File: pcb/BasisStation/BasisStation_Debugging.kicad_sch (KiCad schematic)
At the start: 2 parts, among them J1 USB_B_Micro, U1 D3V3XA4B10LP

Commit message: v0.00.001 chore(SHBS-4): Symbole aus Bibliothek aktualisiert
KiCad-Lauf "Symbole aus Bibliothek aktualisieren" (Bediener): die zuvor per
Text-Edit erzeugte power:+3V3-Cache-Definition wurde durch das
Bibliotheksoriginal ersetzt (abweichende Referenz-Position, Pfeil aus zwei
Polylines), lib_symbols alphabetisch sortiert.

Laut report.txt aktualisieren #PWR100-#PWR102 (power:+3V3), PS1
(shbs_power:MP2359DJ) und J_PWR1 (shbs_power:USB_C_Receptacle_Power)
fehlerfrei - die Bibliotheksentkopplung aus da60c97 traegt.

ERC: 29 -> 14 Meldungen (4 Fehler, 10 Warnungen). Die verbleibenden Fehler
sind ausschliesslich power_pin_not_driven an U6.2, PS1.5, J_PWR1.A4 und
#PWR100 und haengen an PWR_FLAG/Buck-Topologie (SHBS-4 offen).

Co-Authored-By: Claude Opus 5 <noreply@anthropic.com>
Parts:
- U1: footprint Package_DFN_QFN:Diodes_UDFN-10_1.0x2.5mm_P0.5mm -> Package_DFN_QFN:Diodes_UDFN-10_1x2.5mm_P0.5mm
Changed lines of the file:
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@@
 			)
 		)
-		(property "Footprint" "Package_DFN_QFN:Diodes_UDFN-10_1.0x2.5mm_P0.5mm"
+		(property "Footprint" "Package_DFN_QFN:Diodes_UDFN-10_1x2.5mm_P0.5mm"
 			(at 67.31 119.38 0)
 			(effects
@@
 			)
 		)
-		(property "Description" "4-Channel Low Capacitance TVS Diode Array, DFN-10"
+		(property "Description" "4-Channel Low Capacitance TVS Diode Array, DFN-10 / USON-10"
 			(at 91.44 109.22 0)
 			(effects

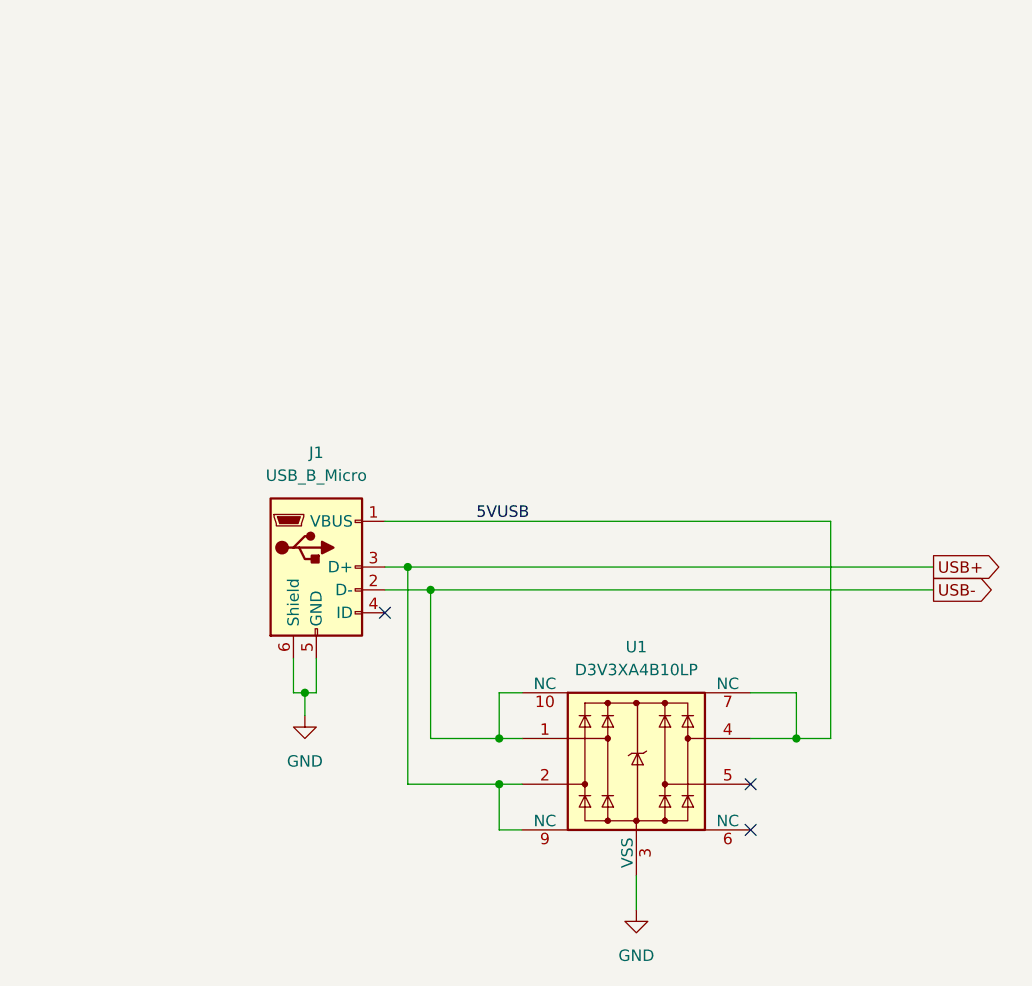
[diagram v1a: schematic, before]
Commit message: v0.00.001 feat(SHBS-6): Debug-Anschluss J1 von USB-B-Micro auf USB-C umgestellt
J1 durch Connector:USB_C_Receptacle_USB2.0_16P ersetzt, bestueckt mit der
Amphenol 12401548E4-2A - derselben Buchse wie der Versorgungsport J_PWR1,
also ohne zusaetzliche BOM-Position.

Beide Datenpaare (A6/B6 und A7/B7) gebrueckt, damit der Stecker in beiden
Orientierungen funktioniert. CC1/CC2 mit je 5,1 kOhm Rd gegen GND (R21, R22)
fuer Sink-Betrieb. Footprint zugewiesen, Netz 5VUSB in VBUS_J1 umbenannt.
VBUS bleibt unbeschaltet - Versorgung laeuft weiterhin ausschliesslich ueber
J_PWR1.

Der GND-Pin des alten USB_B_Micro-Symbols war als Power output deklariert
und damit unbemerkt der einzige ERC-Treiber des globalen GND-Netzes.
Ersetzt durch PWR_FLAG #FLG04 am GND-Draht von J_PWR1.A1.

ERC: 0 Fehler, 9 Warnungen (saemtlich Altbestand).

Co-Authored-By: Claude Opus 5 <noreply@anthropic.com>
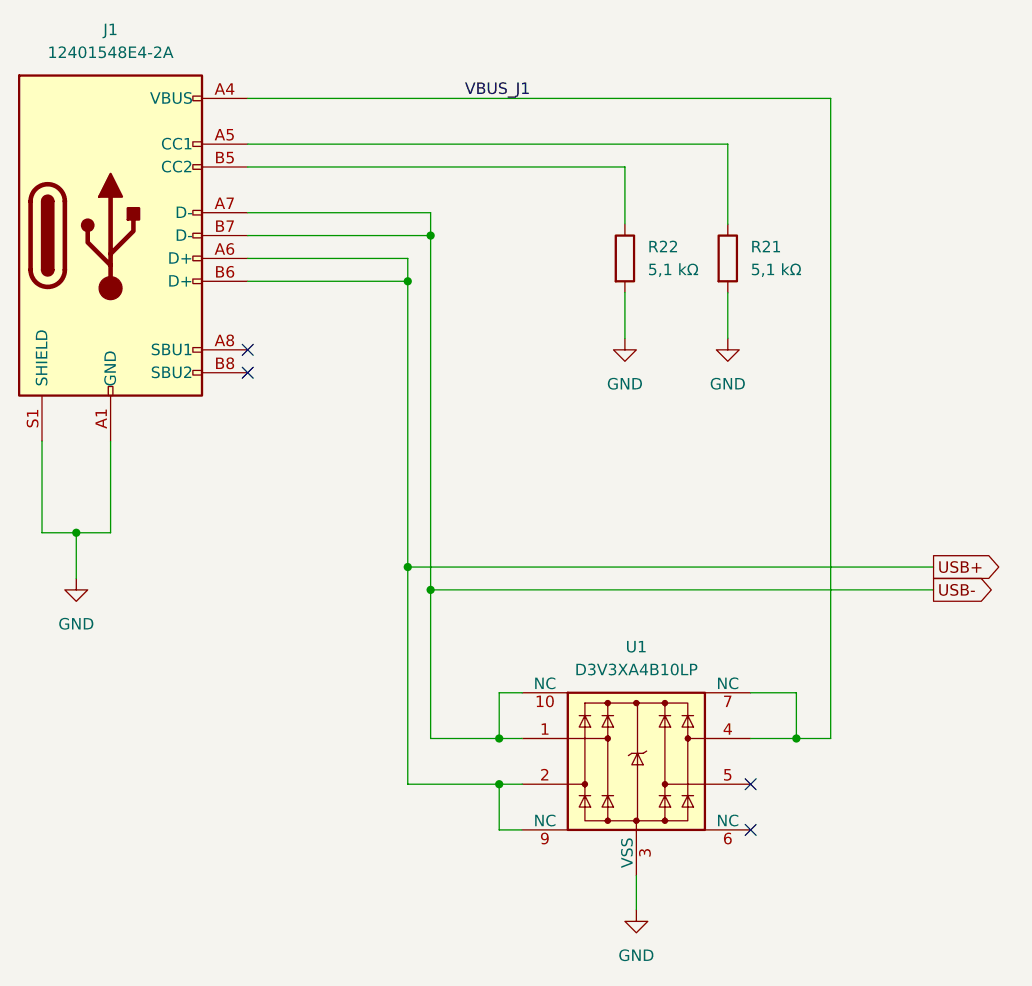
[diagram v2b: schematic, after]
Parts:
- removed J1: USB_B_Micro, symbol Connector:USB_B_Micro
- added J1: 12401548E4-2A, Footprints:USB_C_Receptacle_Amphenol_12401548E4-2A, symbol Connector:USB_C_Receptacle_USB2.0_16P
- added R21, R22: 5,1 kΩ, Resistor_SMD:R_0805_2012Metric, symbol Device:R
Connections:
- net GND: now also J1.A1 (GND), J1.A12 (GND), J1.B1 (GND), J1.B12 (GND), J1.S1 (SHIELD), R21.2, R22.2
- net USB+: now also J1.A6 (D+), J1.B6 (D+)
- net USB-: now also J1.A7 (D-), J1.B7 (D-)
- net 5VUSB renamed VBUS_J1
- net VBUS_J1: now also J1.A4 (VBUS), J1.A9 (VBUS), J1.B4 (VBUS), J1.B9 (VBUS)
- new net: J1.A5 (CC1), R21.1
- new net: J1.B5 (CC2), R22.1
- no-connect marks 3 -> 4

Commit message: v0.00.001 refactor(SHBS-12): KiCad-Bibliotheken auf Bauteilordner umgestellt
Symbol, Footprint und 3D-Modell eines Bauteils lagen bisher in drei
getrennten Sammelordnern. Jedes Bauteil hat jetzt einen eigenen Ordner
unter pcb/Bauteile/; pcb/Symbol/, pcb/Footprints/ und pcb/3D-Model/
entfallen.

Umfang: 20 Dateien verschoben, 13 verwaiste entfernt, 63 Footprint-
Referenzen in Schaltplaenen, Netzliste und Board umgeschrieben, 7
Footprint-Vorgaben in den Symbol-Dateien angepasst.

Nebenbei behoben:
- Die 3D-Modelle waren im Board ueber absolute Pfade auf E: und in der
  Netzliste auf C: verdrahtet, funktionsfaehig jeweils nur auf einem
  Rechner. Jetzt durchgaengig ueber ${KIPRJMOD}.
- Drei Footprint-Referenzen zeigten auf Bibliotheken, die nie in der
  fp-lib-table standen.
- WCAP-FTXX_P10 hatte keine Footprint-Vorgabe, der W5500-Footprint keine
  3D-Referenz.
- fp-info-cache und *.kicad_prl sind nicht mehr versioniert.

Verifikation: Projekt oeffnet ohne Bibliotheks-Warnung. ERC 0 Fehler und
7 Warnungen, vorher 9, keine neue. DRC meldet "Found 0 Footprint errors";
der verbliebene DRC-Fehler ist eine vorbestehende Routing-Luecke im
EN-Netz. 3D-Ansicht zeigt die Modelle.

Co-Authored-By: Claude Opus 5 <noreply@anthropic.com>
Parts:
- J1: footprint Footprints:USB_C_Receptacle_Amphenol_12401548E4-2A -> shbs_power:USB_C_Receptacle_Amphenol_12401548E4-2A
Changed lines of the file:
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@@
 			)
 		)
-		(property "Footprint" "Footprints:USB_C_Receptacle_Amphenol_12401548E4-2A"
+		(property "Footprint" "shbs_power:USB_C_Receptacle_Amphenol_12401548E4-2A"
 			(at 36.83 50.8 0)
 			(effects

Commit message: v0.00.001 feat(SHBS-17): USB-C-Buchse auf 12401598E4#2A umgestellt, Ersatz fuer PS1 vorgeschlagen
J1 und J_PWR1: Die abgekuendigte Amphenol 12401548E4#2A ist durch den
Nachfolger 12401598E4#2A ersetzt. Die neue Buchse ist nicht pad-kompatibel:
die B-Reihe ist SMD statt THT. Padbild aus dem Amphenol-STEP-Modell
ermittelt, es deckt sich mit dem KiCad-Footprint der Schwester
12401610E4-2A; uebernommen als shbs_power:USB_C_Receptacle_Amphenol_
12401598E4-2A. Schaltplan, Symbol-Cache und power.kicad_sym umgestellt,
ERC 0 Fehler.

PS1: Diodes AP3211KTR-G1 als pinkompatibler Ersatz fuer den MP2359
(NRND, ohne Lager) in der Stueckliste vorgeschlagen, Schaltplan noch
unveraendert. Alle 46 Positionen lieferbar, 47,78 EUR pro Baugruppe.

Co-Authored-By: Claude Opus 5.5 <noreply@anthropic.com>
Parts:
- J1: value 12401548E4-2A -> 12401598E4-2A; footprint shbs_power:USB_C_Receptacle_Amphenol_12401548E4-2A -> shbs_power:USB_C_Receptacle_Amphenol_12401598E4-2A; Manufacturer_Part_Number 12401548E4#2A -> 12401598E4#2A; Mouser Part Number 640-12401548E42A -> 523-12401598E4#2A; Notes Alternative: GCT USB4110-GF-A (verify land pattern before s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 -> Successor of discontinued 12401548E4#2A (SHBS-17); land pat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
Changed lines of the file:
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@@
 			)
 		)
-		(property "Value" "12401548E4-2A"
+		(property "Value" "12401598E4-2A"
 			(at 33.02 30.48 0)
 			(effects
@@
 			)
 		)
-		(property "Footprint" "shbs_power:USB_C_Receptacle_Amphenol_12401548E4-2A"
+		(property "Footprint" "shbs_power:USB_C_Receptacle_Amphenol_12401598E4-2A"
 			(at 36.83 50.8 0)
 			(effects
@@
 			)
 		)
-		(property "Manufacturer_Part_Number" "12401548E4#2A"
+		(property "Manufacturer_Part_Number" "12401598E4#2A"
 			(at 33.02 50.8 0)
 			(effects
@@
 			)
 		)
-		(property "Mouser Part Number" "640-12401548E42A"
+		(property "Mouser Part Number" "523-12401598E4#2A"
 			(at 33.02 50.8 0)
 			(effects
@@
 			)
 		)
-		(property "Notes" "Alternative: GCT USB4110-GF-A (verify land pattern before swap)"
+		(property "Notes" "Successor of discontinued 12401548E4#2A (SHBS-17); land pattern checked against Amphenol STEP model"
 			(at 33.02 50.8 0)
 			(effects

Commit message: v0.00.001 feat(SHBS-17): Teilenummern fuer 29 Positionen in den Schaltplan uebernommen
Die vom Bediener freigegebenen Teilevorschlaege (Hausstandard Passivteile, LEDs, Q1-Q4, F1, FB1) stehen jetzt als Felder Manufacturer, Manufacturer_Part_Number und Mouser Part Number an 58 Instanzen. F1-Wert von Fuse auf 1.1A gesetzt. Gegenprobe: keine Felder verloren, Netzliste identisch (102 Netze), ERC 0 Fehler.

Stueckliste gruppiert jetzt nach Herstellerteilenummer (Werte sind uneinheitlich geschrieben): 44 Positionen, alle lieferbar, 47,78 EUR. PROPOSED_PARTS geleert, Hausstandard in hardware.md dokumentiert, Bestellteile in power_supply.md aktualisiert.

Co-Authored-By: Claude Opus 5.5 <noreply@anthropic.com>
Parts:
- R21, R22: Manufacturer (none) -> YAGEO; Manufacturer_Part_Number (none) -> RC0805FR-075K1L; Mouser Part Number (none) -> 603-RC0805FR-075K1L
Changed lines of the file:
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@@
+			)
+		)
+		(property "Manufacturer" "YAGEO"
+			(at 101.6 53.34 0)
+			(effects
+				(font
+					(size 1.27 1.27)
+				)
+				(hide yes)
+			)
+		)
+		(property "Manufacturer_Part_Number" "RC0805FR-075K1L"
+			(at 101.6 53.34 0)
+			(effects
+				(font
+					(size 1.27 1.27)
+				)
+				(hide yes)
+			)
+		)
+		(property "Mouser Part Number" "603-RC0805FR-075K1L"
+			(at 101.6 53.34 0)
+			(effects
+				(font
+					(size 1.27 1.27)
+				)
+				(hide yes)
 			)
 		)
@@
 			(at 90.17 53.34 0)
 			(effects
+				(font
+					(size 1.27 1.27)
+				)
+				(hide yes)
+			)
+		)
+		(property "Manufacturer" "YAGEO"
+			(at 90.17 53.34 0)
+			(effects
+				(font
+					(size 1.27 1.27)
+				)
+				(hide yes)
+			)
+		)
+		(property "Manufacturer_Part_Number" "RC0805FR-075K1L"
+			(at 90.17 53.34 0)
+			(effects
+				(font
+					(size 1.27 1.27)
+				)
+				(hide yes)
+			)
+		)
+		(property "Mouser Part Number" "603-RC0805FR-075K1L"
+			(at 90.17 53.34 0)
+			(effects

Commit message: v0.00.001 feat(SHBS-17): Abgeleitete Teilenummern bestaetigt und eingetragen, SHBS-17 abgeschlossen
D11 Comchip SS34-HF (SMA; die guenstigere Slkormicro-SS34 ist SMC und passt nicht auf D_SMA), D12 Littelfuse SMAJ5.0A, U1 D3V3XA4B10LP-7, L1 Bourns SRN6045TA-100M, J6 Wuerth 61200621621 als Felder im Schaltplan. DERIVED_PART_NUMBERS geleert. DigiKey-Stichwortsuche bevorzugt den Hersteller aus dem Schaltplan statt des billigsten Doppelgaengers. Netzliste identisch, ERC 0 Fehler. Stueckliste: 44 Positionen, alle eindeutig und lieferbar, 48,29 EUR. Task 0041 abgeschlossen; in Task 0042 zwei durch SHBS-17 erledigte Schritte vermerkt.

Co-Authored-By: Claude Opus 5.5 <noreply@anthropic.com>
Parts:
- U1: Manufacturer (none) -> Diodes Incorporated; Manufacturer_Part_Number (none) -> D3V3XA4B10LP-7; Mouser Part Number (none) -> 621-D3V3XA4B10LP-7
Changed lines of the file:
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@@
+			)
+		)
+		(property "Manufacturer" "Diodes Incorporated"
+			(at 91.44 109.22 0)
+			(effects
+				(font
+					(size 1.27 1.27)
+				)
+				(hide yes)
+			)
+		)
+		(property "Manufacturer_Part_Number" "D3V3XA4B10LP-7"
+			(at 91.44 109.22 0)
+			(effects
+				(font
+					(size 1.27 1.27)
+				)
+				(hide yes)
+			)
+		)
+		(property "Mouser Part Number" "621-D3V3XA4B10LP-7"
+			(at 91.44 109.22 0)
+			(effects
+				(font
+					(size 1.27 1.27)
+				)
+				(hide yes)
 			)
 		)

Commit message: v0.00.001 fix(SHBS-38): J1 auf projekteigenes USB-C-Symbol mit Schirm-Pin S1 umgestellt
Co-Authored-By: Claude Opus 5.5 <noreply@anthropic.com>
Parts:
- J1: symbol Connector:USB_C_Receptacle_USB2.0_16P -> shbs_power:USB_C_Receptacle_USB2.0_16P
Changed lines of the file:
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@@
 	)
 	(symbol
-		(lib_id "Connector:USB_C_Receptacle_USB2.0_16P")
+		(lib_id "shbs_power:USB_C_Receptacle_USB2.0_16P")
 		(at 33.02 50.8 0)
 		(unit 1)
